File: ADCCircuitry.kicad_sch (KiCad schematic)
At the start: 22 parts, among them J10 Screw_Terminal_01x02, J9 Screw_Terminal_01x04, U2 ADS112C04, U3 ADS112C04, U4 ADS112C04, U5 ADS112C04

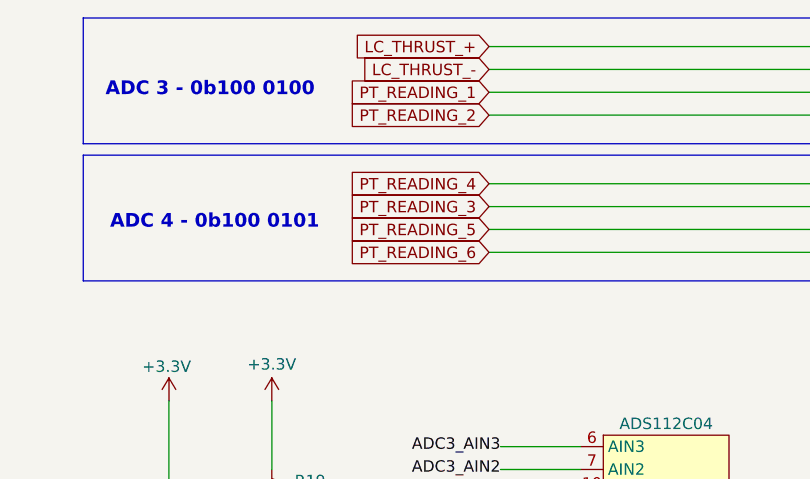
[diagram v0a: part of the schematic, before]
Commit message: Actually fix PT3 and PT4 mapping
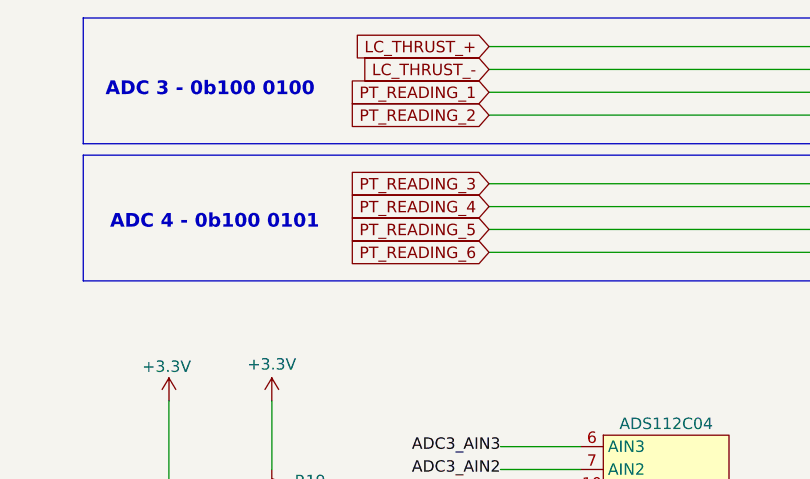
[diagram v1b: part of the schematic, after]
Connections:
- net PT_READING_3: now also U5.6 (AIN3); no longer U5.7 (AIN2)
- net PT_READING_4: now also U5.7 (AIN2); no longer U5.6 (AIN3)
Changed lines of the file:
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@@
+		)
+	)
+	(global_label "PT_READING_6"
+		(shape input)
+		(at 200.66 46.99 180)
+		(fields_autoplaced yes)
+		(effects
+			(font
+				(size 1.27 1.27)
+			)
+			(justify right)
+		)
+		(property "Intersheetrefs" "${INTERSHEET_REFS}"
+			(at 184.3096 46.99 0)
+			(effects
+				(font
+					(size 1.27 1.27)
+				)
+				(justify right)
+				(hide yes)
+			)
+		)
+	)
+	(global_label "LC_THRUST_-"
+		(shape input)
+		(at 200.66 26.67 180)
+		(fields_autoplaced yes)
+		(effects
+			(font
+				(size 1.27 1.27)
+			)
+			(justify right)
+		)
+		(property "Intersheetrefs" "${INTERSHEET_REFS}"
+			(at 184.7934 26.67 0)
+			(effects
+				(font
+					(size 1.27 1.27)
+				)
+				(justify right)
+				(hide yes)
+			)
+		)
+	)
+	(global_label "LC_FILL_-"
+		(shape input)
+		(at 121.92 46.99 180)
+		(fields_autoplaced yes)
+		(effects
+			(font
+				(size 1.27 1.27)
+			)
+			(justify right)
+		)
+		(property "Intersheetrefs" "${INTERSHEET_REFS}"
+			(at 109.3795 46.99 0)
+			(effects
+				(font
+					(size 1.27 1.27)
+				)
+				(justify right)
+				(hide yes)
+			)
 		)
 	)
 	(global_label "PT_READING_3"
 		(shape input)
+		(at 200.66 39.37 180)
+		(fields_autoplaced yes)
+		(effects
+			(font
+				(size 1.27 1.27)
+			)
+			(justify right)
+		)
+		(property "Intersheetrefs" "${INTERSHEET_REFS}"
+			(at 184.3096 39.37 0)
+			(effects
+				(font
+					(size 1.27 1.27)
+				)
+				(justify right)
+				(hide yes)
+			)
+		)
+	)
+	(global_label "PT_READING_2"
+		(shape input)
+		(at 200.66 31.75 180)
+		(fields_autoplaced yes)
+		(effects
+			(font
+				(size 1.27 1.27)
+			)
+			(justify right)
+		)
+		(property "Intersheetrefs" "${INTERSHEET_REFS}"
+			(at 184.3096 31.75 0)
+			(effects
+				(font
+					(size 1.27 1.27)
+				)
+				(justify right)
+				(hide yes)
+			)
+		)
+	)
+	(global_label "LC_FILL_+"
+		(shape input)
+		(at 121.92 44.45 180)
+		(fields_autoplaced yes)
+		(effects
+			(font
+				(size 1.27 1.27)
+			)
+			(justify right)
+		)
+		(property "Intersheetrefs" "${INTERSHEET_REFS}"
+			(at 109.3795 44.45 0)
+			(effects
+				(font
+					(size 1.27 1.27)
+				)
+				(justify right)
+				(hide yes)
+			)
+		)
+	)
+	(global_label "I2C_SDA"
+		(shape input)
+		(at 234.95 128.27 0)
+		(fields_autoplaced yes)
+		(effects
+			(font
+				(size 1.27 1.27)
+			)
+			(justify left)
+		)
+		(property "Intersheetrefs" "${INTERSHEET_REFS}"
+			(at 245.5552 128.27 0)
+			(effects
+				(font
+					(size 1.27 1.27)
+				)
+				(justify left)
+				(hide yes)
+			)
+		)
+	)
+	(global_label "I2C_SDA"
+		(shape input)
+		(at 114.3 77.47 0)
+		(fields_autoplaced yes)
+		(effects
+			(font
+				(size 1.27 1.27)
+			)
+			(justify left)
+		)
+		(property "Intersheetrefs" "${INTERSHEET_REFS}"
+			(at 124.9052 77.47 0)
+			(effects
+				(font
+					(size 1.27 1.27)
+				)
+				(justify left)
+				(hide yes)
+			)
+		)
+	)
+	(global_label "I2C_SCL"
+		(shape input)
+		(at 234.95 125.73 0)
+		(fields_autoplaced yes)
+		(effects
+			(font
+				(size 1.27 1.27)
+			)
+			(justify left)
+		)
+		(property "Intersheetrefs" "${INTERSHEET_REFS}"
+			(at 245.4947 125.73 0)
+			(effects
+				(font
+					(size 1.27 1.27)
+				)
+				(justify left)
+				(hide yes)
+			)
+		)
+	)
+	(global_label "I2C_DRDY_ADC3"
+		(shape input)
+		(at 259.08 81.28 0)
+		(fields_autoplaced yes)
+		(effects
+			(font
+				(size 1.27 1.27)
+			)
+			(justify left)
+		)
+		(property "Intersheetrefs" "${INTERSHEET_REFS}"
+			(at 276.8214 81.28 0)
+			(effects
+				(font
+					(size 1.27 1.27)
+				)
+				(justify left)
+				(hide yes)
+			)
+		)
+	)
+	(global_label "I2C_DRDY_ADC2"
+		(shape input)
+		(at 133.35 132.08 0)
+		(fields_autoplaced yes)
+		(effects
+			(font
+				(size 1.27 1.27)
+			)
+			(justify left)
+		)
+		(property "Intersheetrefs" "${INTERSHEET_REFS}"
+			(at 151.0914 132.08 0)
+			(effects
+				(font
+					(size 1.27 1.27)
+				)
+				(justify left)
+				(hide yes)
+			)
+		)
+	)
+	(global_label "PT_READING_4"
+		(shape input)
 		(at 200.66 41.91 180)
 		(fields_autoplaced yes)
@@
 				(hide yes)
 			)
-		)
-	)
-	(global_label "PT_READING_6"
-		(shape input)
-		(at 200.66 46.99 180)
-		(fields_autoplaced yes)
-		(effects
-			(font
-				(size 1.27 1.27)
-			)
-			(justify right)
-		)
-		(property "Intersheetrefs" "${INTERSHEET_REFS}"
-			(at 184.3096 46.99 0)
-			(effects
-				(font
-					(size 1.27 1.27)
-				)
-				(justify right)
-				(hide yes)
-			)
-		)
-	)
-	(global_label "LC_THRUST_-"
-		(shape input)
-		(at 200.66 26.67 180)
-		(fields_autoplaced yes)
-		(effects
-			(font
-				(size 1.27 1.27)
-			)
-			(justify right)
-		)
-		(property "Intersheetrefs" "${INTERSHEET_REFS}"
-			(at 184.7934 26.67 0)
-			(effects
-				(font
-					(size 1.27 1.27)
-				)
-				(justify right)
-				(hide yes)
-			)
-		)
-	)
-	(global_label "LC_FILL_-"
-		(shape input)
-		(at 121.92 46.99 180)
-		(fields_autoplaced yes)
-		(effects
-			(font
-				(size 1.27 1.27)
-			)
-			(justify right)
-		)
-		(property "Intersheetrefs" "${INTERSHEET_REFS}"
-			(at 109.3795 46.99 0)
-			(effects
-				(font
-					(size 1.27 1.27)
-				)
-				(justify right)
-				(hide yes)
-			)
-		)
-	)
-	(global_label "PT_READING_2"
-		(shape input)
-		(at 200.66 31.75 180)
-		(fields_autoplaced yes)
-		(effects
-			(font
-				(size 1.27 1.27)
-			)
-			(justify right)
-		)
-		(property "Intersheetrefs" "${INTERSHEET_REFS}"
-			(at 184.3096 31.75 0)
-			(effects
-				(font
-					(size 1.27 1.27)
-				)
-				(justify right)
-				(hide yes)
-			)
-		)
-	)
-	(global_label "LC_FILL_+"
-		(shape input)
-		(at 121.92 44.45 180)
-		(fields_autoplaced yes)
-		(effects
-			(font
-				(size 1.27 1.27)
-			)
-			(justify right)
-		)
-		(property "Intersheetrefs" "${INTERSHEET_REFS}"
-			(at 109.3795 44.45 0)
-			(effects
-				(font
-					(size 1.27 1.27)
-				)
-				(justify right)
-				(hide yes)
-			)
-		)
-	)
-	(global_label "I2C_SDA"
-		(shape input)
-		(at 234.95 128.27 0)
-		(fields_autoplaced yes)
-		(effects
-			(font
-				(size 1.27 1.27)
-			)
-			(justify left)
-		)
-		(property "Intersheetrefs" "${INTERSHEET_REFS}"
-			(at 245.5552 128.27 0)
-			(effects
-				(font
-					(size 1.27 1.27)
-				)
-				(justify left)
-				(hide yes)
-			)
-		)
-	)
-	(global_label "I2C_SDA"
-		(shape input)
-		(at 114.3 77.47 0)
-		(fields_autoplaced yes)
-		(effects
-			(font
-				(size 1.27 1.27)
-			)
-			(justify left)
-		)
-		(property "Intersheetrefs" "${INTERSHEET_REFS}"
-			(at 124.9052 77.47 0)
-			(effects
-				(font
-					(size 1.27 1.27)
-				)
-				(justify left)
-				(hide yes)
-			)
-		)
-	)
-	(global_label "I2C_SCL"
-		(shape input)
-		(at 234.95 125.73 0)
-		(fields_autoplaced yes)
-		(effects
-			(font
-				(size 1.27 1.27)
-			)
-			(justify left)
-		)
-		(property "Intersheetrefs" "${INTERSHEET_REFS}"
-			(at 245.4947 125.73 0)
-			(effects
-				(font
-					(size 1.27 1.27)
-				)
-				(justify left)
-				(hide yes)
-			)
-		)
-	)
-	(global_label "PT_READING_4"
-		(shape input)
-		(at 200.66 39.37 180)
-		(fields_autoplaced yes)
-		(effects
-			(font
-				(size 1.27 1.27)
-			)
-			(justify right)
-		)
-		(property "Intersheetrefs" "${INTERSHEET_REFS}"
-			(at 184.3096 39.37 0)
-			(effects
-				(font
-					(size 1.27 1.27)
-				)
-				(justify right)
-				(hide yes)
-			)
-		)
-	)
-	(global_label "I2C_DRDY_ADC3"
-		(shape input)
-		(at 259.08 81.28 0)
-		(fields_autoplaced yes)
-		(effects
-			(font
-				(size 1.27 1.27)
-			)
-			(justify left)
-		)
-		(property "Intersheetrefs" "${INTERSHEET_REFS}"
-			(at 276.8214 81.28 0)
-			(effects
-				(font
-					(size 1.27 1.27)
-				)
-				(justify left)
-				(hide yes)
-			)
-		)
-	)
-	(global_label "I2C_DRDY_ADC2"
-		(shape input)
-		(at 133.35 132.08 0)
-		(fields_autoplaced yes)
-		(effects
-			(font
-				(size 1.27 1.27)
-			)
-			(justify left)
-		)
-		(property "Intersheetrefs" "${INTERSHEET_REFS}"
-			(at 151.0914 132.08 0)
-			(effects
-				(font
-					(size 1.27 1.27)
-				)
-				(justify left)
-				(hide yes)
-			)

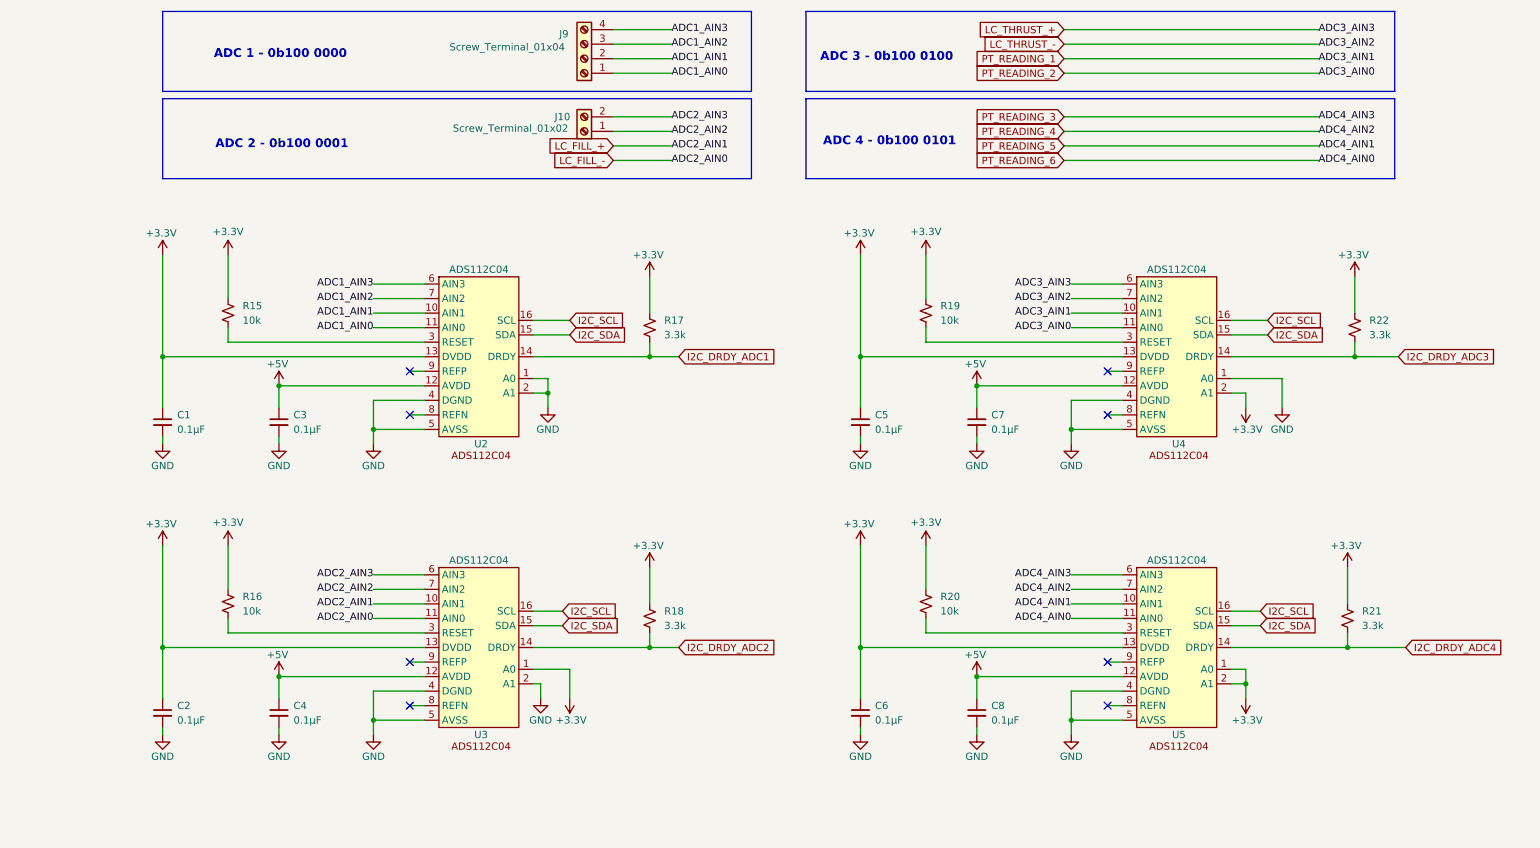
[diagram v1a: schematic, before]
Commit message: Add signal conditioning. Change screw hole footprint
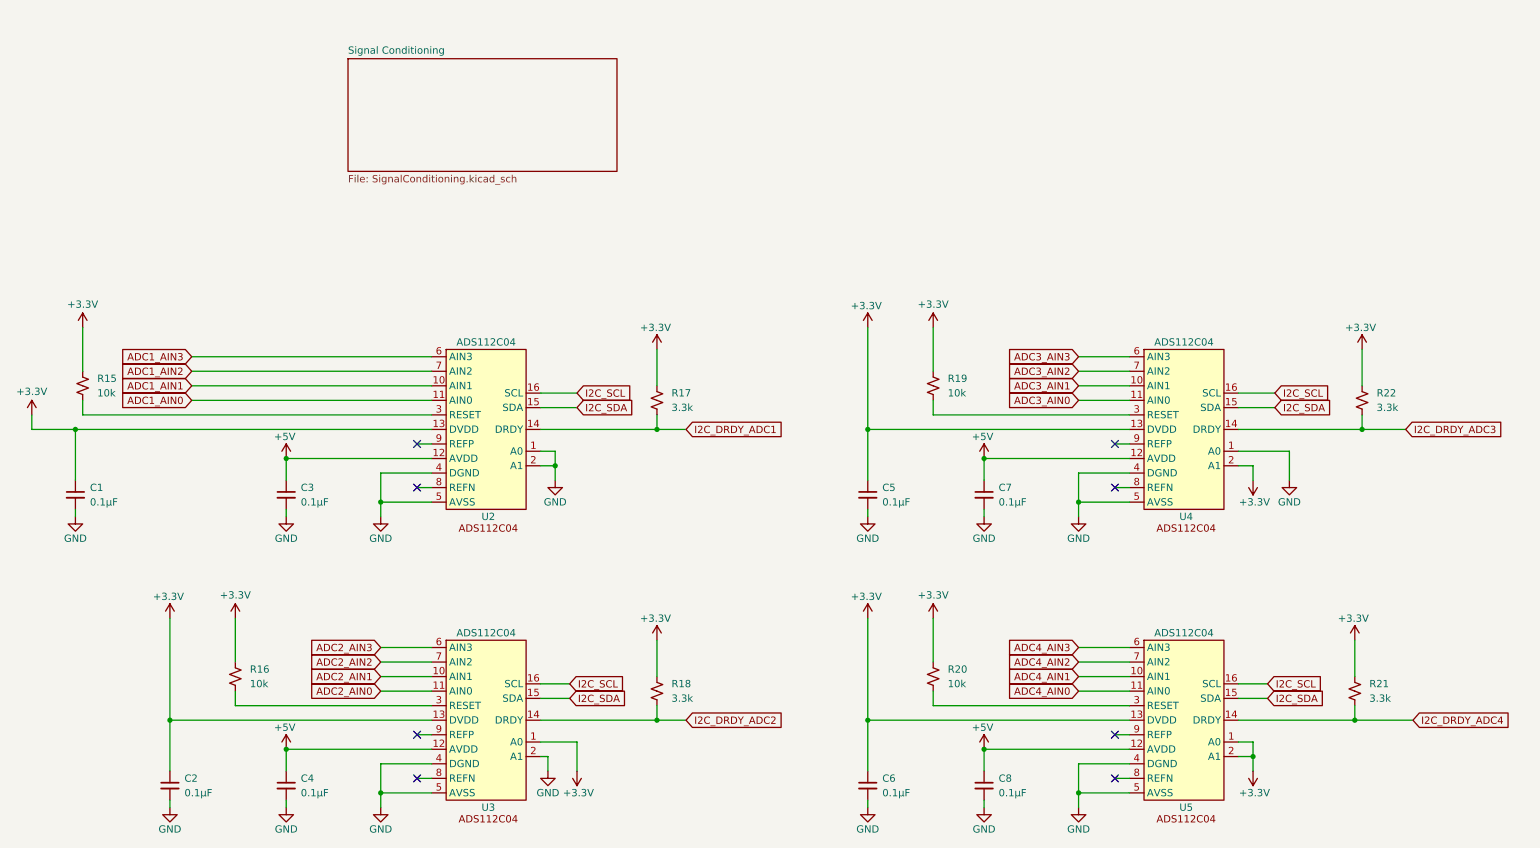
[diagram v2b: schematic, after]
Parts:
- removed J10: Screw_Terminal_01x02, TerminalBlock:TerminalBlock_Xinya_XY308-2.54-2P_1x02_P2.54mm_Horizontal, symbol Connector:Screw_Terminal_01x02
- removed J9: Screw_Terminal_01x04, TerminalBlock:TerminalBlock_Xinya_XY308-2.54-4P_1x04_P2.54mm_Horizontal, symbol Connector:Screw_Terminal_01x04
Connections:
- net LC_FILL_+ renamed ADC2_AIN1
- net LC_FILL_- renamed ADC2_AIN0
- net LC_THRUST_+ renamed ADC3_AIN3
- net LC_THRUST_- renamed ADC3_AIN2
- net PT_READING_1 renamed ADC3_AIN1
- net PT_READING_2 renamed ADC3_AIN0
- net PT_READING_3 renamed ADC4_AIN3
- net PT_READING_4 renamed ADC4_AIN2
- net PT_READING_5 renamed ADC4_AIN1
- net PT_READING_6 renamed ADC4_AIN0
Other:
- added sheet Signal Conditioning (SignalConditioning.kicad_sch)
- note removed: "ADC 1 - 0b100 0000"
- note removed: "ADC 2 - 0b100 0001"
- note removed: "ADC 3 - 0b100 0100"
- note removed: "ADC 4 - 0b100 0101"
- moved on the sheet: C1, C2, C3, C4, C5, C6, C7, C8, R15, R16, R17, R18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

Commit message: connected to GPIO pins
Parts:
- renumbered C5 to C10, C6 to C11, C7 to C12, C8 to C13, C1 to C6, C2 to C7, C3 to C8, C4 to C9, R15 to R22, R16 to R23, R17 to R24, R18 to R25, R19 to R26, R20 to R27, R21 to R28, R22 to R29

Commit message: pcb first draft, changed esp32 pin connections
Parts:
- renumbered R22 to R21, R23 to R22, R24 to R23, R25 to R24, R26 to R25, R27 to R26, R28 to R27, R29 to R28
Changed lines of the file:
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@@
 		(dnp no)
 		(fields_autoplaced yes)
-		(property "Reference" "R22"
+		(property "Reference" "R21"
 			(at 31.75 85.0899 0)
 			(effects
@@
 			(project "nexus"
 				(path "/226c5870-4123-4efa-a2b3-b42d02f59bb7/21243b6d-fc9e-4696-b2f4-96a9d8b17f22"
-					(reference "R22")
+					(reference "R21")
 					(unit 1)
 				)
@@
 		(dnp no)
 		(fields_autoplaced yes)
-		(property "Reference" "R26"
+		(property "Reference" "R25"
 			(at 180.34 85.0899 0)
 			(effects
@@
 			(project "nexus"
 				(path "/226c5870-4123-4efa-a2b3-b42d02f59bb7/21243b6d-fc9e-4696-b2f4-96a9d8b17f22"
-					(reference "R26")
+					(reference "R25")
 					(unit 1)
 				)
@@
 		(dnp no)
 		(fields_autoplaced yes)
-		(property "Reference" "R28"
+		(property "Reference" "R27"
 			(at 254 138.4299 0)
 			(effects
@@
 			(project "nexus"
 				(path "/226c5870-4123-4efa-a2b3-b42d02f59bb7/21243b6d-fc9e-4696-b2f4-96a9d8b17f22"
-					(reference "R28")
+					(reference "R27")
 					(unit 1)
 				)
@@
 		(dnp no)
 		(fields_autoplaced yes)
-		(property "Reference" "R27"
+		(property "Reference" "R26"
 			(at 180.34 135.8899 0)
 			(effects
@@
 			(project "nexus"
 				(path "/226c5870-4123-4efa-a2b3-b42d02f59bb7/21243b6d-fc9e-4696-b2f4-96a9d8b17f22"
-					(reference "R27")
+					(reference "R26")
 					(unit 1)
 				)
@@
 		(dnp no)
 		(fields_autoplaced yes)
-		(property "Reference" "R29"
+		(property "Reference" "R28"
 			(at 255.27 87.6299 0)
 			(effects
@@
 			(project "nexus"
 				(path "/226c5870-4123-4efa-a2b3-b42d02f59bb7/21243b6d-fc9e-4696-b2f4-96a9d8b17f22"
-					(reference "R29")
+					(reference "R28")
 					(unit 1)
 				)
@@
 		(dnp no)
 		(fields_autoplaced yes)
-		(property "Reference" "R23"
+		(property "Reference" "R22"
 			(at 58.42 135.8899 0)
 			(effects
@@
 			(project "nexus"
 				(path "/226c5870-4123-4efa-a2b3-b42d02f59bb7/21243b6d-fc9e-4696-b2f4-96a9d8b17f22"
-					(reference "R23")
+					(reference "R22")
 					(unit 1)
 				)
@@
 		(dnp no)
 		(fields_autoplaced yes)
-		(property "Reference" "R24"
+		(property "Reference" "R23"
 			(at 132.08 87.6299 0)
 			(effects
@@
 			(project "nexus"
 				(path "/226c5870-4123-4efa-a2b3-b42d02f59bb7/21243b6d-fc9e-4696-b2f4-96a9d8b17f22"
-					(reference "R24")
+					(reference "R23")
 					(unit 1)
 				)
@@
 		(dnp no)
 		(fields_autoplaced yes)
-		(property "Reference" "R25"
+		(property "Reference" "R24"
 			(at 132.08 138.4299 0)
 			(effects
@@
 			(project "nexus"
 				(path "/226c5870-4123-4efa-a2b3-b42d02f59bb7/21243b6d-fc9e-4696-b2f4-96a9d8b17f22"
-					(reference "R25")
+					(reference "R24")
 					(unit 1)
 				)
